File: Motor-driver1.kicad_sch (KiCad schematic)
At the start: 30 parts, among them J8 PINHD_1x4_Male, J9 PINHD_1x4_Male, U2 DRV8825PWP, U3 DRV8825PWP

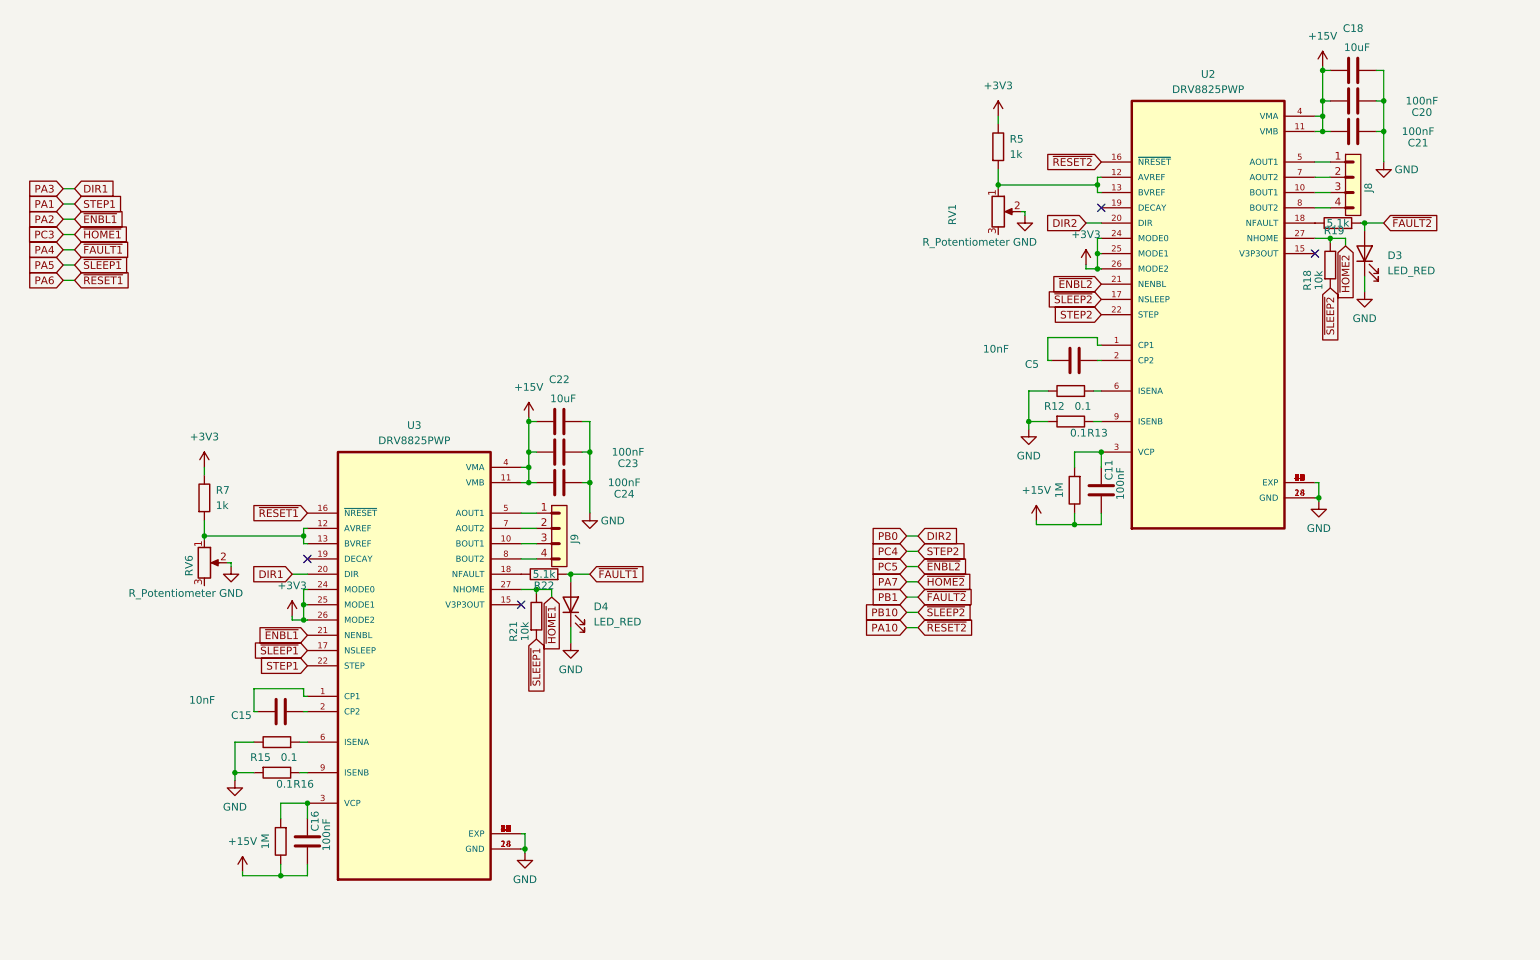
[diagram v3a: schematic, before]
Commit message: added pins for motor edge sensors, reroutet driver modules, removed module potentiometer, made everything more compact, fixed labels
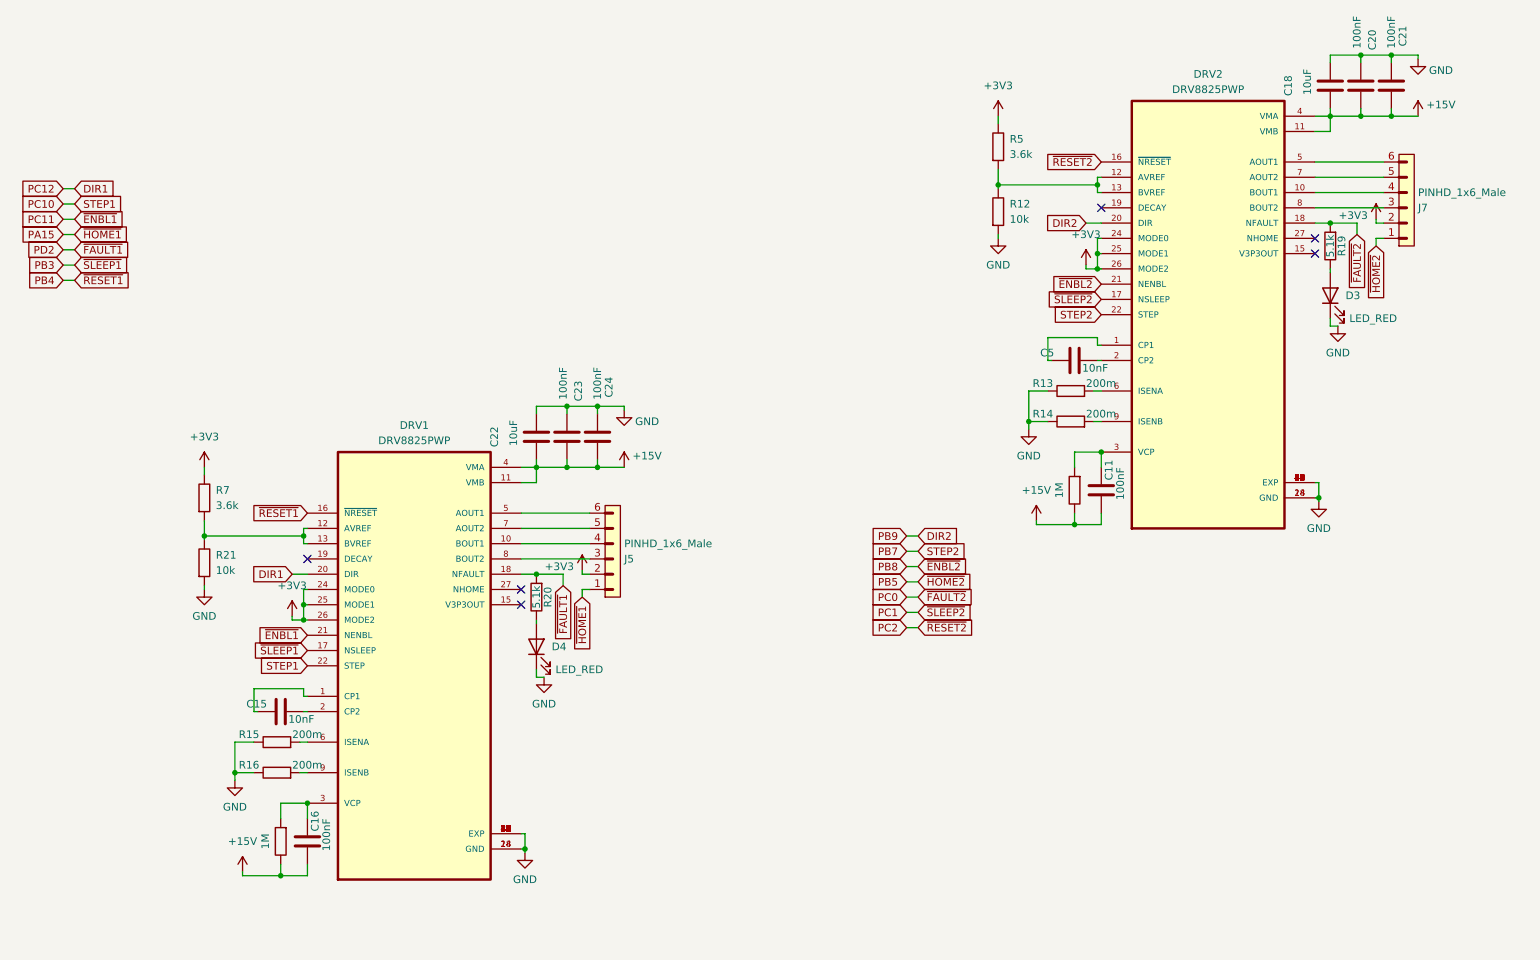
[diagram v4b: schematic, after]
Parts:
- removed J8, J9: PINHD_1x4_Male, Connector_PinHeader_2.54mm:PinHeader_1x04_P2.54mm_Vertical, symbol PCM_SL_Pin_Headers:PINHD_1x4_Male
- removed R22: 5.1k, Resistor_SMD:R_0805_2012Metric, symbol PCM_SL_Devices:Resistor
- removed RV1, RV6: R_Potentiometer, poti:3386P1473LF, symbol Device:R_Potentiometer
- added J5, J7: PINHD_1x6_Male, Connector_PinHeader_2.54mm:PinHeader_1x06_P2.54mm_Vertical, symbol PCM_SL_Pin_Headers:PINHD_1x6_Male
- added R20: 5.1k, Resistor_SMD:R_0805_2012Metric, symbol PCM_SL_Devices:Resistor
- R12: value 0.1 -> 10k; footprint Resistor_SMD:R_1206_3216Metric -> Resistor_SMD:R_0805_2012Metric
- R13, R15, R16: value 0.1 -> 200m; footprint Resistor_SMD:R_1206_3216Metric -> Resistor_SMD:R_0402_1005Metric
- R14: value 1M -> 200m; footprint Resistor_SMD:R_0805_2012Metric -> Resistor_SMD:R_0402_1005Metric
- R18: value 10k -> 1M
- R5, R7: value 1k -> 3.6k
- renumbered U3 to DRV1, U2 to DRV2
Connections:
- net +15V: now also R18.2; no longer R14.2
- net +3V3: now also J5.2, J7.2
- net GND: now also R12.1, R13.2, R14.2, R16.2, R21.1; no longer R12.2, R13.1, R16.1
- net at DRV1.5 (AOUT1): now also J5.6
- net at DRV1.7 (AOUT2): now also J5.5
- net at DRV1.10 (BOUT1): now also J5.4
- net at DRV1.8 (BOUT2): now also J5.3
- net at DRV1.12 (AVREF), DRV1.13 (BVREF), R7.1: now also R21.2
- net at DRV2.9 (ISENB): now also R14.1; no longer R13.2
- net at DRV2.12 (AVREF), DRV2.13 (BVREF), R5.1: now also R12.2
- net at R19.2: now also D3.2 (A); no longer DRV2.18 (NFAULT)
- net PD2: now reaches DRV1.18 (NFAULT)
- net PD2: now also R20.1
- net at DRV2.10 (BOUT1): now also J7.4
- net at C11.2, DRV2.3 (VCP): now also R18.1; no longer R14.1
- net at DRV2.5 (AOUT1): now also J7.6
- net at DRV2.6 (ISENA): now also R13.1; no longer R12.1
- net at DRV2.7 (AOUT2): now also J7.5
- net at DRV2.8 (BOUT2): now also J7.3
- net at DRV1.9 (ISENB): now also R16.1; no longer R16.2
- net PA1 renamed PC10
- net PA10 renamed PC2
- net PA2 renamed PC11
- net PA4: no longer names the net of D4.2 (A)
- net PA4: now also R20.2
- net PA5 renamed PB3
- net PB3: no longer R21.1
- net PA6 renamed PB4
- net PA7: no longer names the net of DRV2.27 (NHOME)
- net PA7: no longer R18.2
- net PB1 renamed PC0
- net PC0: now also DRV2.18 (NFAULT); no longer D3.2 (A)
- net PB10 renamed PC1
- net PC1: no longer R18.1
- net PC3: no longer names the net of DRV1.27 (NHOME)
- net PC3: no longer R21.2
- net PC4 renamed PB7
- net PC5 renamed PB8
- new net PA15: J5.1
- new net PB5: J7.1
- no-connect marks 4 -> 6
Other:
- moved on the sheet: C22, C23, C24

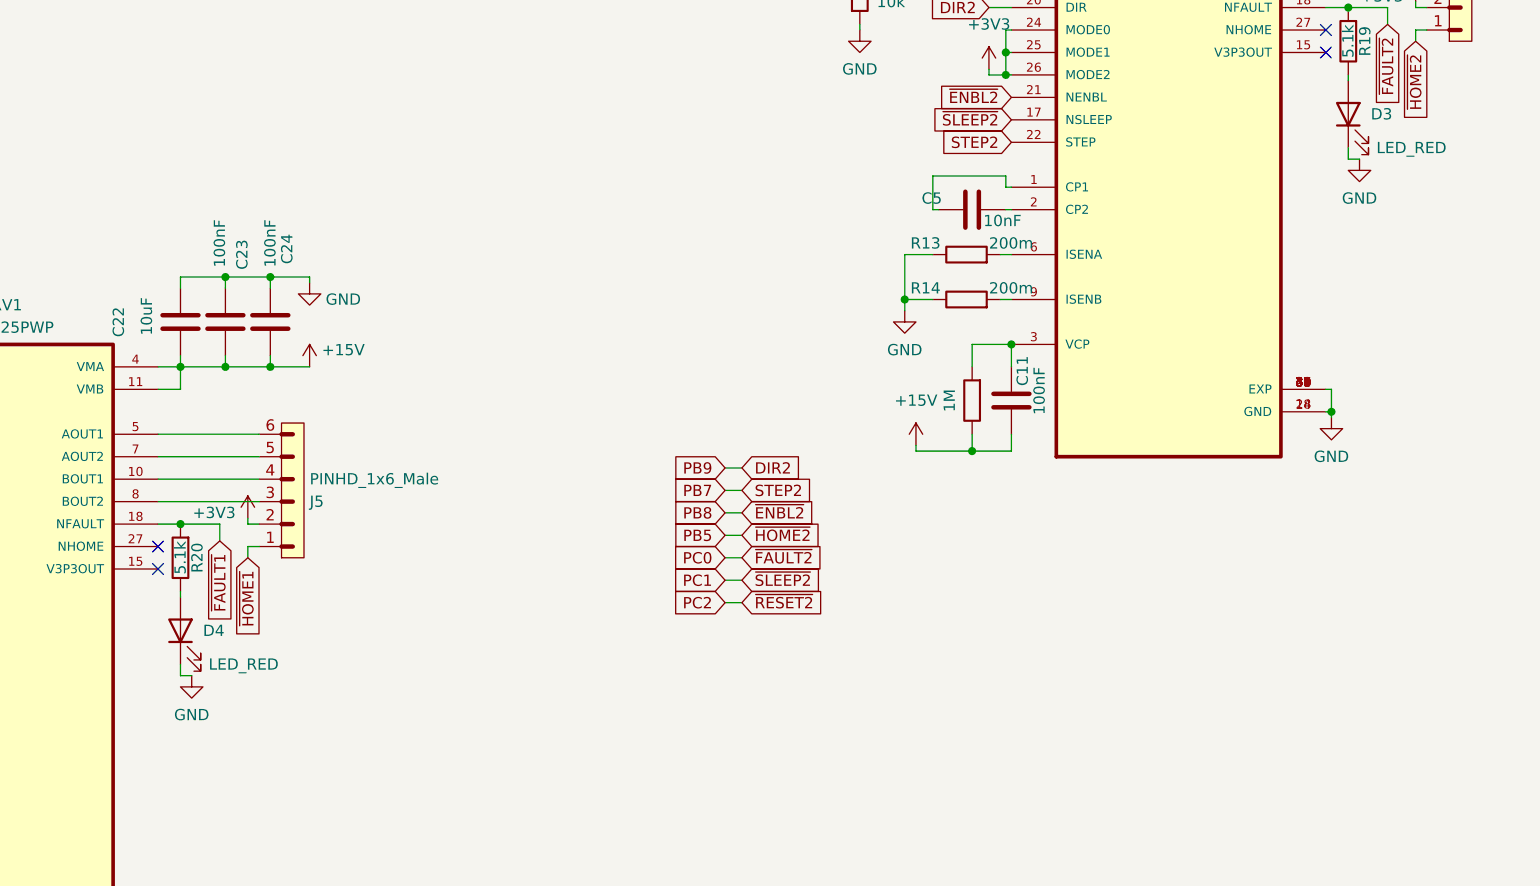
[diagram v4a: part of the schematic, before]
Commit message: fixed Serial connection, and various improvments
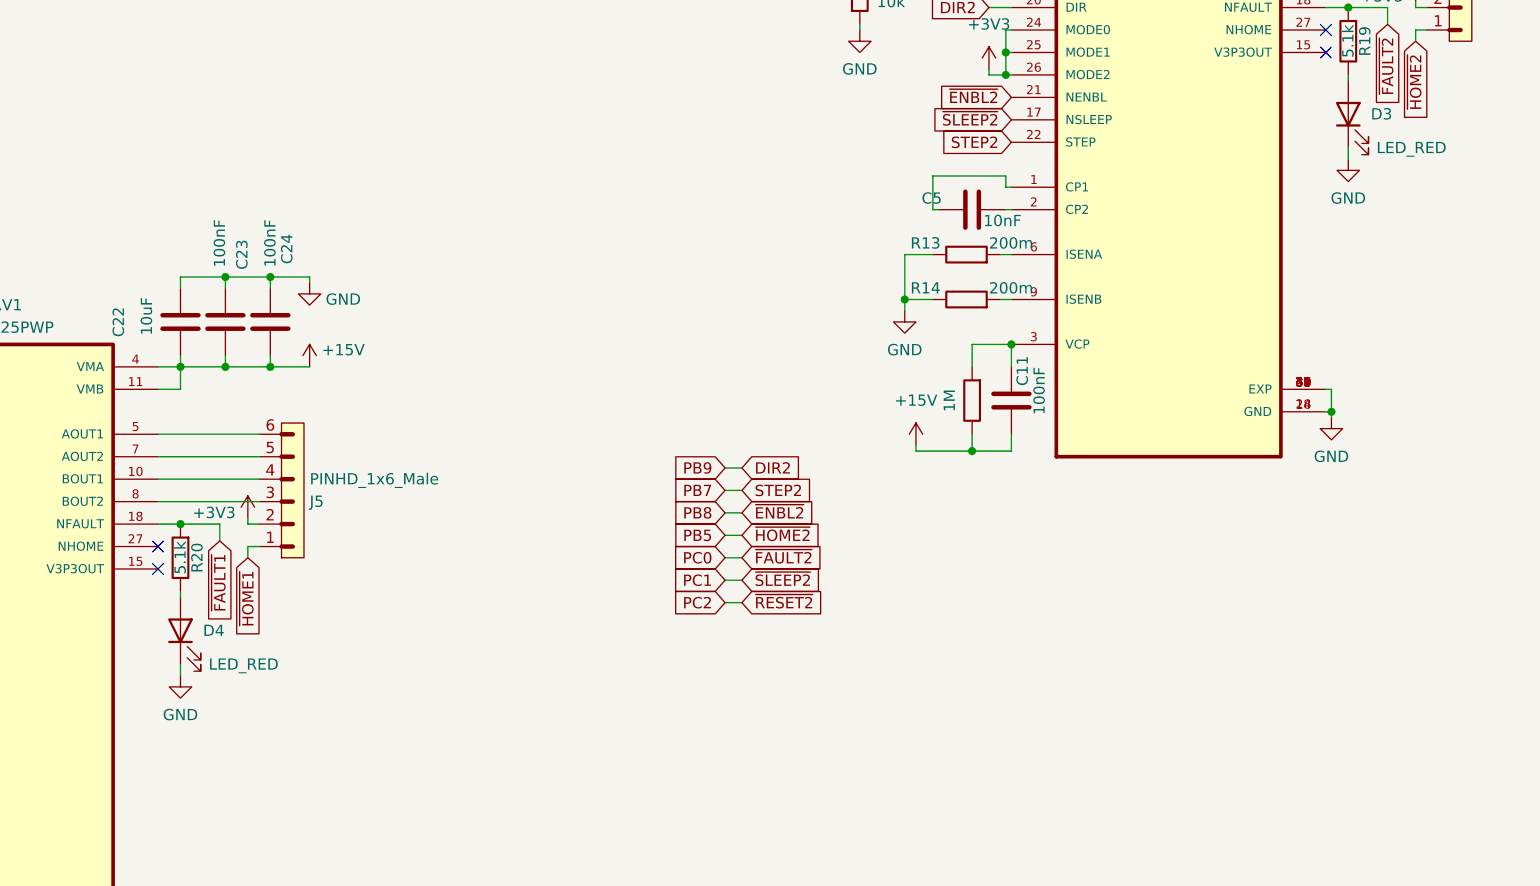
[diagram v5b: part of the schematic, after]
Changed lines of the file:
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@@
-    (stroke (width 0) (type default))
-  )
-  (wire (pts (xy 125.095 135.255) (xy 126.365 135.255))
     (stroke (width 0) (type default))
   )
@@
   )
   (wire (pts (xy 214.63 100.33) (xy 214.63 97.79))
-    (stroke (width 0) (type default))
-  )
-  (wire (pts (xy 257.175 76.835) (xy 258.445 76.835))
     (stroke (width 0) (type default))
   )
@@
     )
   )
-  (symbol (lib_id "power:GND") (at 258.445 76.835 0) (unit 1)
+  (symbol (lib_id "power:GND") (at 257.175 76.835 0) (unit 1)
     (in_bom yes) (on_board yes) (dnp no) (fields_autoplaced)
-    (property "Reference" "#PWR047" (at 258.445 83.185 0)
-      (effects (font (size 1.27 1.27)) hide)
-    )
-    (property "Value" "GND" (at 258.445 81.28 0)
-      (effects (font (size 1.27 1.27)))
-    )
-    (property "Footprint" "" (at 258.445 76.835 0)
-      (effects (font (size 1.27 1.27)) hide)
-    )
-    (property "Datasheet" "" (at 258.445 76.835 0)
+    (property "Reference" "#PWR047" (at 257.175 83.185 0)
+      (effects (font (size 1.27 1.27)) hide)
+    )
+    (property "Value" "GND" (at 257.175 81.28 0)
+      (effects (font (size 1.27 1.27)))
+    )
+    (property "Footprint" "" (at 257.175 76.835 0)
+      (effects (font (size 1.27 1.27)) hide)
+    )
+    (property "Datasheet" "" (at 257.175 76.835 0)
       (effects (font (size 1.27 1.27)) hide)
     )
@@
     )
   )
-  (symbol (lib_id "power:GND") (at 126.365 135.255 0) (unit 1)
+  (symbol (lib_id "power:GND") (at 125.095 135.255 0) (unit 1)
     (in_bom yes) (on_board yes) (dnp no) (fields_autoplaced)
-    (property "Reference" "#PWR033" (at 126.365 141.605 0)
-      (effects (font (size 1.27 1.27)) hide)
-    )
-    (property "Value" "GND" (at 126.365 139.7 0)
-      (effects (font (size 1.27 1.27)))
-    )
-    (property "Footprint" "" (at 126.365 135.255 0)
-      (effects (font (size 1.27 1.27)) hide)
-    )
-    (property "Datasheet" "" (at 126.365 135.255 0)
-      (effects (font (size 1.27 1.27)) hide)
-    )
+    (property "Reference" "#PWR033" (at 125.095 141.605 0)
+      (effects (font (size 1.27 1.27)) hide)
+    )
+    (property "Value" "GND" (at 125.095 139.7 0)
+      (effects (font (size 1.27 1.27)))
+    )
+    (property "Footprint" "" (at 125.095 135.255 0)
+      (effects (font (size 1.27 1.27)) hide)
+    )
+    (property "Datasheet" "" (at 125.095 135.255 0)
+      (effects (font (size 1.27 1.27)) hide)
+    )
